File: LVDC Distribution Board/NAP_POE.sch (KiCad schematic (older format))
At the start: 0 parts

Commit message: Inputs / Outputs Reallyyyy Done
These two schematic sections are very finalized now. Time to do the power conversion section : - )
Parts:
- added J? (x2): RJ45_LED_Shielded, symbol Connector:RJ45_LED_Shielded
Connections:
- new net: J?.1, J?.1
- new net: J?.2, J?.2
- new net: J?.3, J?.3
- new net: J?.6, J?.6
- new net GND: J?.7, J?.8, J?.SH, J?.SH
- new net LP24V: J?.4, J?.5
- no-connect marks 0 -> 4
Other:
- note added: "NAP PoE"
- note added: "Should probably light the green LED on startup,\nas a debugging "she got power bys" check"
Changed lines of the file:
@@
 $Descr A4 11693 8268
 encoding utf-8
-Sheet 1 7
+Sheet 4 7
 Title ""
 Date ""
@@
 Comment4 ""
 $EndDescr
+Text Notes 8350 6960 0    197  Italic 39
+NAP PoE
+$Comp
+L Connector:RJ45_LED_Shielded J?
+U 1 1 5C650637
+P 6680 4150
+F 0 "J?" H 6680 4817 50  0000 C CNN
+F 1 "RJ45_LED_Shielded" H 6680 4726 50  0000 C CNN
+F 2 "" V 6680 4175 50  0001 C CNN
+F 3 "~" V 6680 4175 50  0001 C CNN
+	1    6680 4150
+	-1   0    0    1
+$EndComp
+$Comp
+L Connector:RJ45_LED_Shielded J?
+U 1 1 5C650693
+P 6670 2430
+F 0 "J?" H 6670 3097 50  0000 C CNN
+F 1 "RJ45_LED_Shielded" H 6670 3006 50  0000 C CNN
+F 2 "" V 6670 2455 50  0001 C CNN
+F 3 "~" V 6670 2455 50  0001 C CNN
+	1    6670 2430
+	-1   0    0    1
+$EndComp
+$Comp
+L power:GND #PWR?
+U 1 1 5C650810
+P 6890 3510
+F 0 "#PWR?" H 6890 3260 50  0001 C CNN
+F 1 "GND" H 6895 3337 50  0000 C CNN
+F 2 "" H 6890 3510 50  0001 C CNN
+F 3 "" H 6890 3510 50  0001 C CNN
+	1    6890 3510
+	1    0    0    -1
+$EndComp
+$Comp
+L power:GND #PWR?
+U 1 1 5C65082E
+P 6920 1760
+F 0 "#PWR?" H 6920 1510 50  0001 C CNN
+F 1 "GND" H 6925 1587 50  0000 C CNN
+F 2 "" H 6920 1760 50  0001 C CNN
+F 3 "" H 6920 1760 50  0001 C CNN
+	1    6920 1760
+	1    0    0    -1
+$EndComp
+Wire Wire Line
+	6890 3510 6890 3480
+Wire Wire Line
+	6890 3480 6680 3480
+Wire Wire Line
+	6680 3480 6680 3650
+Wire Wire Line
+	6920 1760 6920 1710
+Wire Wire Line
+	6920 1710 6670 1710
+Wire Wire Line
+	6670 1710 6670 1930
+NoConn ~ 6270 2830
+NoConn ~ 6270 2730
+NoConn ~ 6270 2530
+NoConn ~ 6270 2430
+Wire Wire Line
+	6270 2630 5910 2630
+Wire Wire Line
+	5910 2630 5910 4350
+Wire Wire Line
+	5910 4350 6280 4350
+Wire Wire Line
+	6270 2330 5940 2330
+Wire Wire Line
+	5940 2330 5940 4050
+Wire Wire Line
+	5940 4050 6280 4050
+Wire Wire Line
+	6270 2230 5980 2230
+Wire Wire Line
+	5980 2230 5980 3950
+Wire Wire Line
+	5980 3950 6280 3950
+Wire Wire Line
+	6270 2130 6020 2130
+Wire Wire Line
+	6020 2130 6020 3850
+Wire Wire Line
+	6020 3850 6280 3850
+Wire Wire Line
+	6280 4450 6180 4450
+Wire Wire Line
+	6180 4450 6180 4550
+Wire Wire Line
+	6180 4550 6280 4550
+Wire Wire Line
+	6180 4550 6180 4710
+Connection ~ 6180 4550
+$Comp
+L power:GND #PWR?
+U 1 1 5C65173A
+P 6180 4710
+F 0 "#PWR?" H 6180 4460 50  0001 C CNN
+F 1 "GND" H 6185 4537 50  0000 C CNN
+F 2 "" H 6180 4710 50  0001 C CNN
+F 3 "" H 6180 4710 50  0001 C CNN
+	1    6180 4710
+	1    0    0    -1
+$EndComp
+Wire Wire Line
+	6280 4150 6200 4150
+Wire Wire Line
+	6200 4150 6200 4250
+Wire Wire Line
+	6200 4250 6280 4250
+Wire Wire Line
+	6200 4150 4410 4150
+Connection ~ 6200 4150
+Text HLabel 4410 4150 0    50   Input ~ 0
+LP24V
+Text Notes 7230 2220 0    50   ~ 0
+Should probably light the green LED on startup,\nas a debugging "she got power bys" check
 $EndSCHEMATC

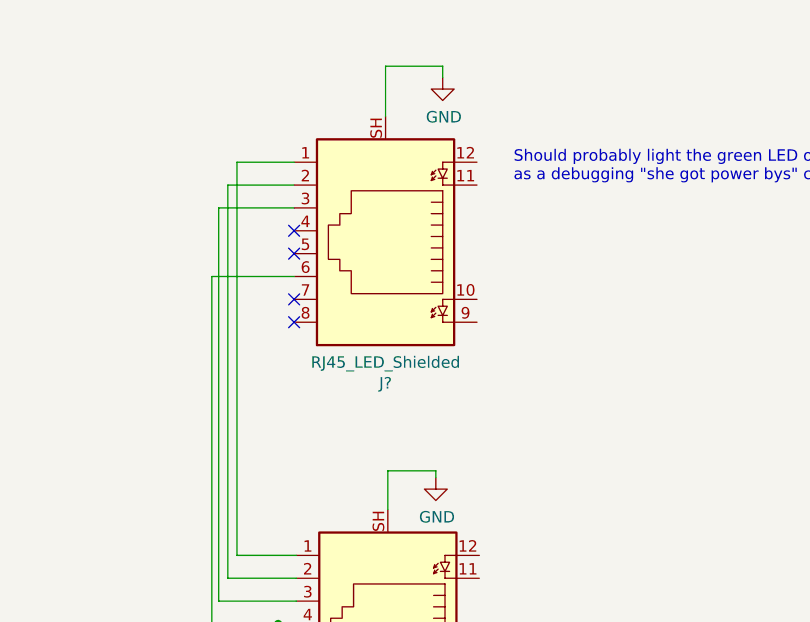
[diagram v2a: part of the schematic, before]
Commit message: SAMD21 Added
-Added VSense on rails
-Added SAMD21 and related circuits
-Mapped signals to the uC.
-Hope this is a better commit description
-Hi Frank
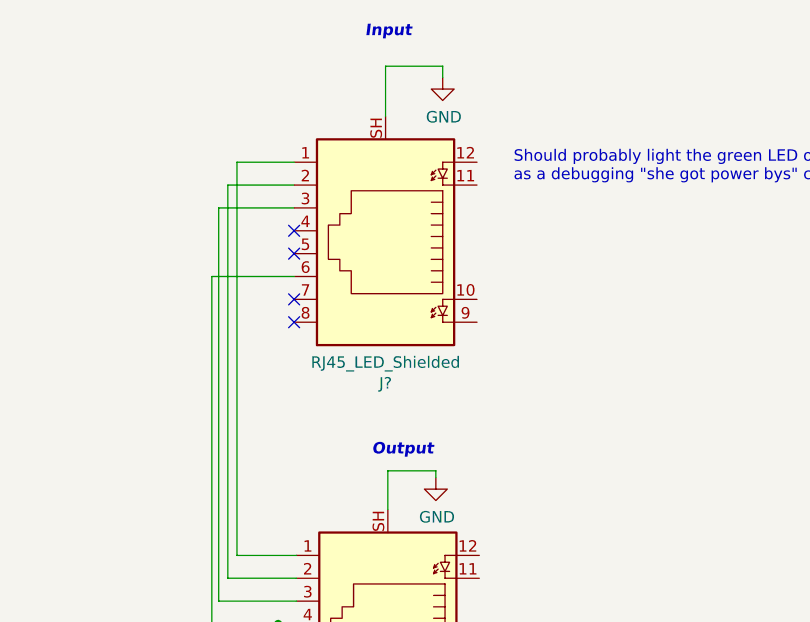
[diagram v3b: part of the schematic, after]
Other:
- note added: "Input"
- note added: "Output"
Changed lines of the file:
@@
 $EndComp
 $Comp
-L power:GND #PWR?
+L power:GND #PWR0128
 U 1 1 5C650810
 P 6890 3510
-F 0 "#PWR?" H 6890 3260 50  0001 C CNN
+F 0 "#PWR0128" H 6890 3260 50  0001 C CNN
 F 1 "GND" H 6895 3337 50  0000 C CNN
 F 2 "" H 6890 3510 50  0001 C CNN
@@
 $EndComp
 $Comp
-L power:GND #PWR?
+L power:GND #PWR0129
 U 1 1 5C65082E
 P 6920 1760
-F 0 "#PWR?" H 6920 1510 50  0001 C CNN
+F 0 "#PWR0129" H 6920 1510 50  0001 C CNN
 F 1 "GND" H 6925 1587 50  0000 C CNN
 F 2 "" H 6920 1760 50  0001 C CNN
@@
 Connection ~ 6180 4550
 $Comp
-L power:GND #PWR?
+L power:GND #PWR0130
 U 1 1 5C65173A
 P 6180 4710
-F 0 "#PWR?" H 6180 4460 50  0001 C CNN
+F 0 "#PWR0130" H 6180 4460 50  0001 C CNN
 F 1 "GND" H 6185 4537 50  0000 C CNN
 F 2 "" H 6180 4710 50  0001 C CNN
@@
 Text Notes 7230 2220 0    50   ~ 0
 Should probably light the green LED on startup,\nas a debugging "she got power bys" check
+Text Notes 6580 1590 0    50   Italic 10
+Input
+Text Notes 6610 3420 0    50   Italic 10
+Output
 $EndSCHEMATC

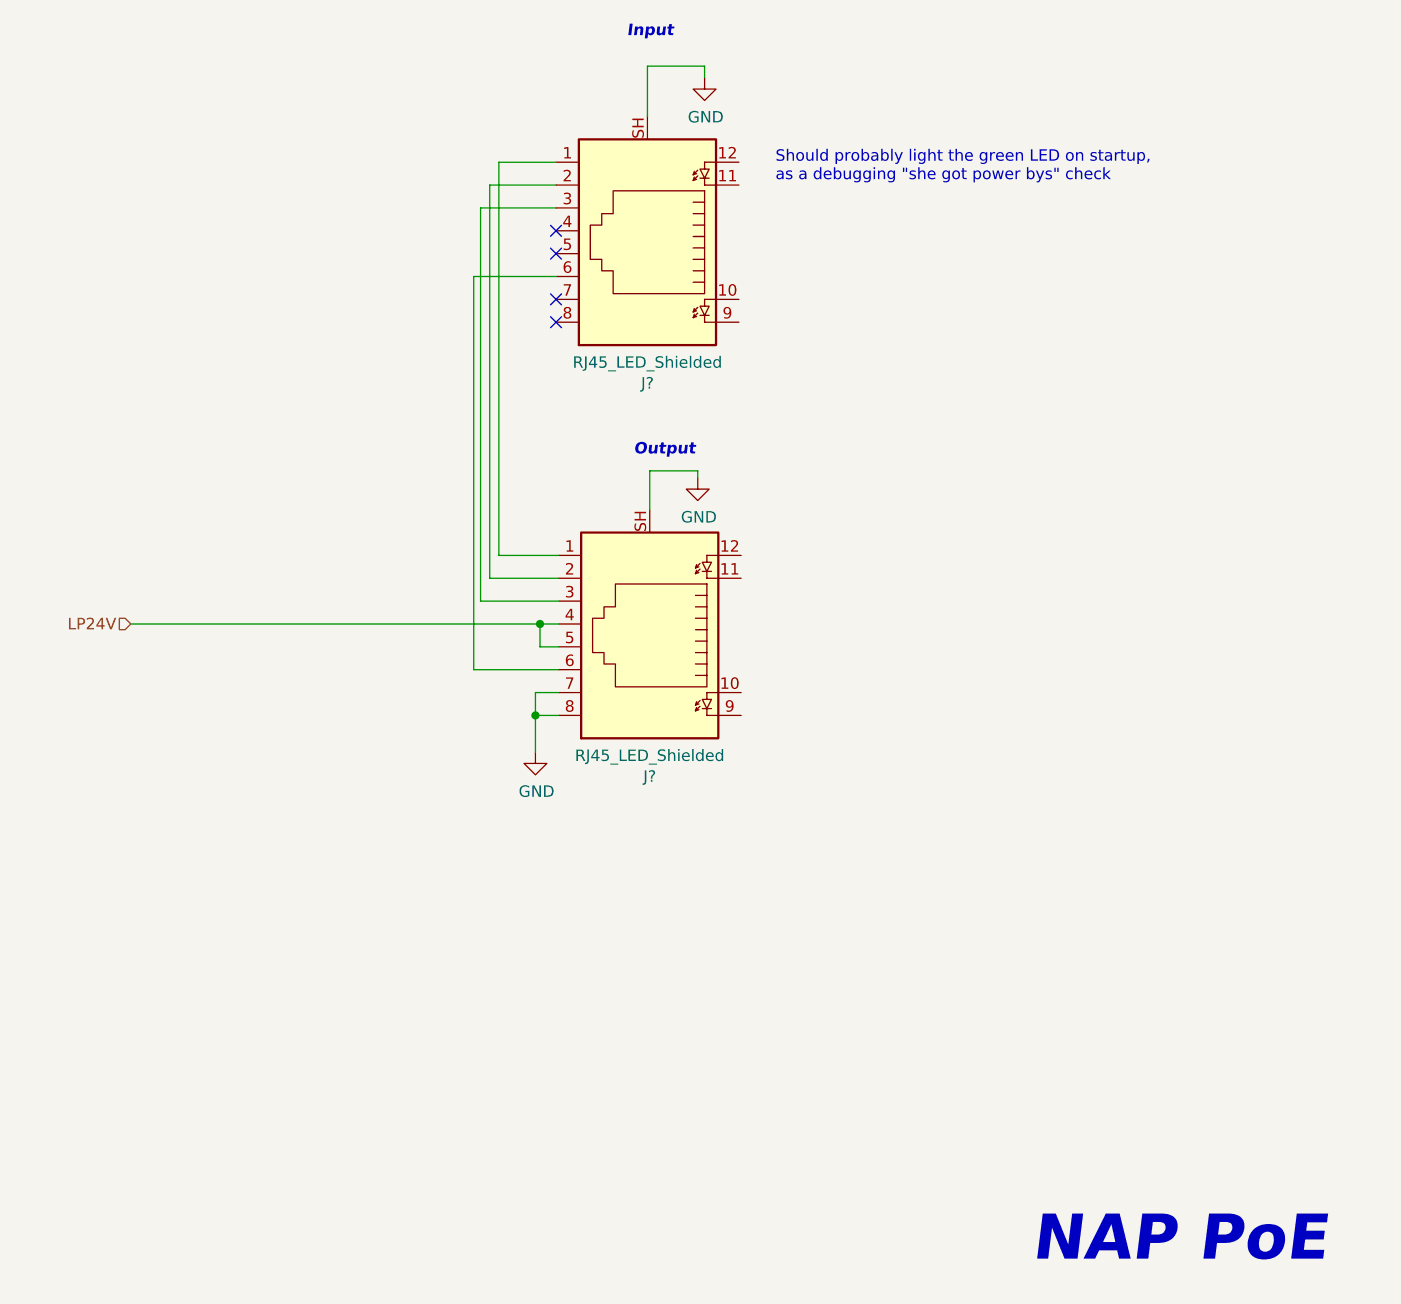
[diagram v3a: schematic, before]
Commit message: Schematic "Done"
-Added Wiznet legacy n0de schematic
-Cleaned up schematic in general
-Other than minor changes, the schematic is finalized.
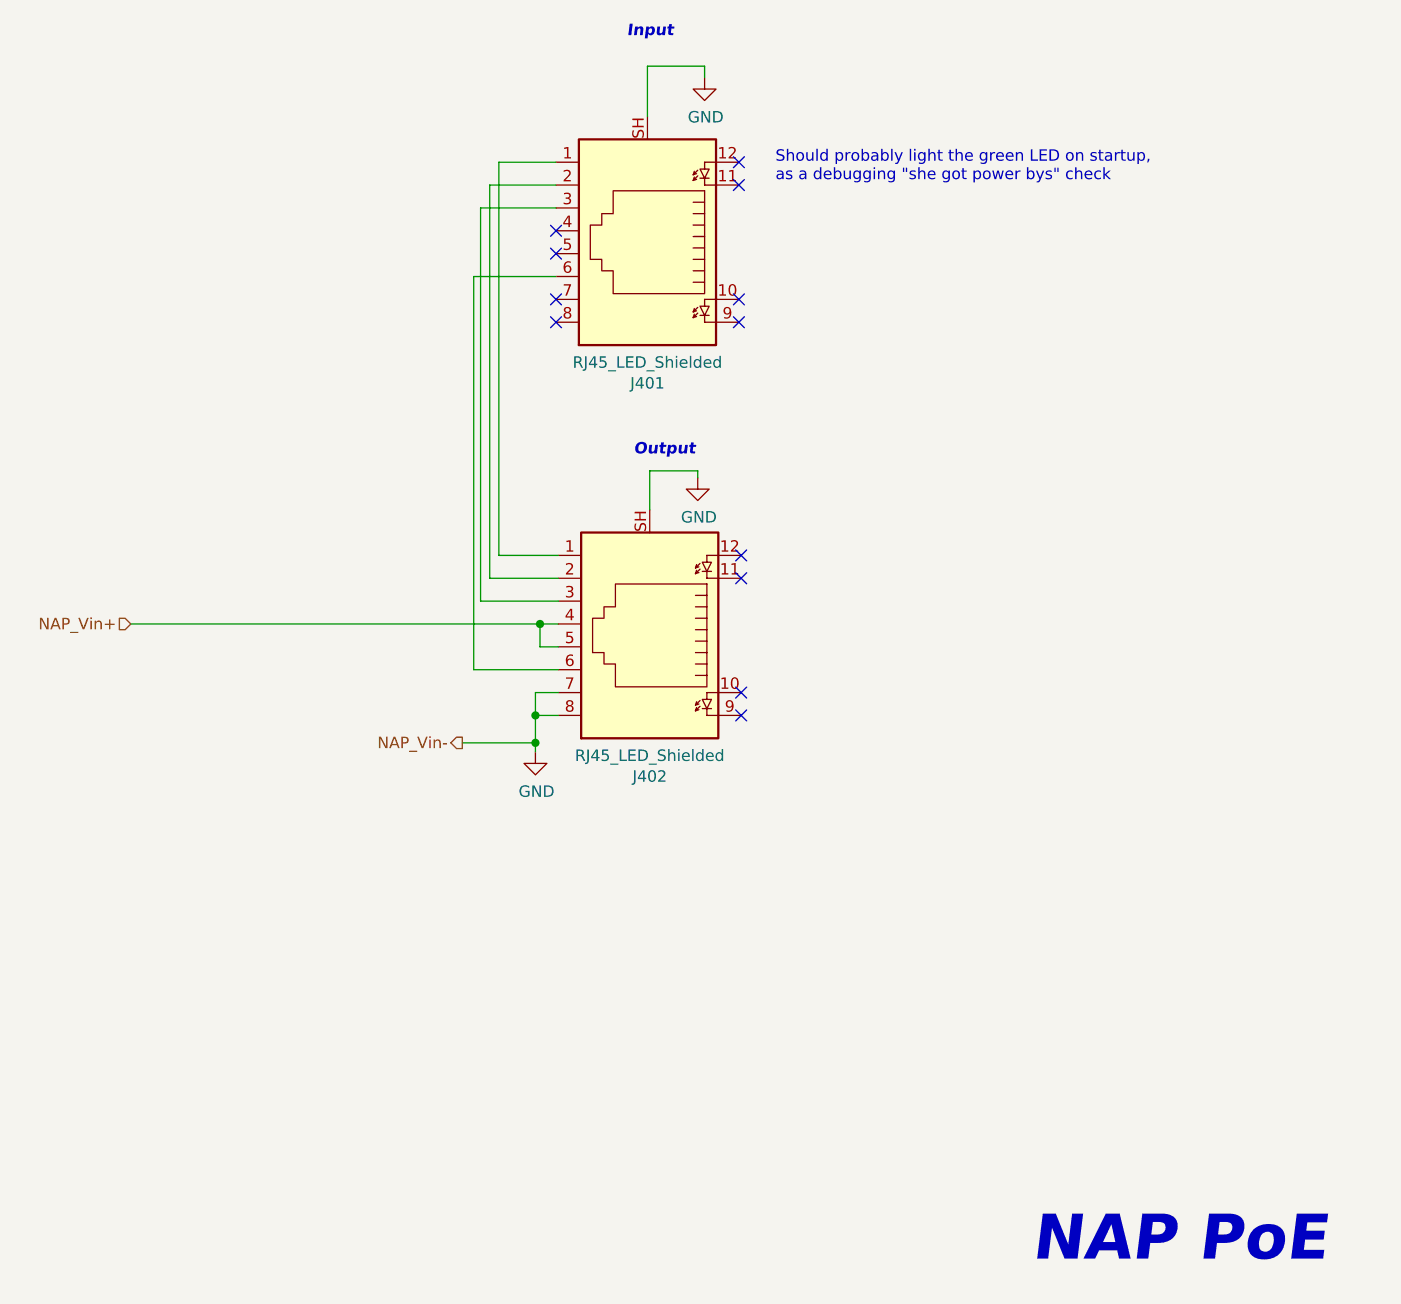
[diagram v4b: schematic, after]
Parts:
- gave numbers to parts that had none: 2
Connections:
- net LP24V renamed NAP_Vin+
- no-connect marks 4 -> 12
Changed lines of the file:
@@
 NAP PoE
 $Comp
-L Connector:RJ45_LED_Shielded J?
+L Connector:RJ45_LED_Shielded J402
 U 1 1 5C650637
 P 6680 4150
-F 0 "J?" H 6680 4817 50  0000 C CNN
+F 0 "J402" H 6680 4817 50  0000 C CNN
 F 1 "RJ45_LED_Shielded" H 6680 4726 50  0000 C CNN
 F 2 "" V 6680 4175 50  0001 C CNN
@@
 $EndComp
 $Comp
-L Connector:RJ45_LED_Shielded J?
+L Connector:RJ45_LED_Shielded J401
 U 1 1 5C650693
 P 6670 2430
-F 0 "J?" H 6670 3097 50  0000 C CNN
+F 0 "J401" H 6670 3097 50  0000 C CNN
 F 1 "RJ45_LED_Shielded" H 6670 3006 50  0000 C CNN
 F 2 "" V 6670 2455 50  0001 C CNN
@@
 	6180 4550 6280 4550
 Wire Wire Line
-	6180 4550 6180 4710
+	6180 4550 6180 4670
 Connection ~ 6180 4550
 $Comp
@@
 Connection ~ 6200 4150
 Text HLabel 4410 4150 0    50   Input ~ 0
-LP24V
+NAP_Vin+
 Text Notes 7230 2220 0    50   ~ 0
 Should probably light the green LED on startup,\nas a debugging "she got power bys" check
@@
 Text Notes 6610 3420 0    50   Italic 10
 Output
+Text HLabel 5860 4670 0    50   Output ~ 0
+NAP_Vin-
+Wire Wire Line
+	5860 4670 6180 4670
+Connection ~ 6180 4670
+Wire Wire Line
+	6180 4670 6180 4710
+NoConn ~ 7070 2130
+NoConn ~ 7070 2230
+NoConn ~ 7070 2730
+NoConn ~ 7070 2830
+NoConn ~ 7080 3850
+NoConn ~ 7080 3950
+NoConn ~ 7080 4450
+NoConn ~ 7080 4550
 $EndSCHEMATC

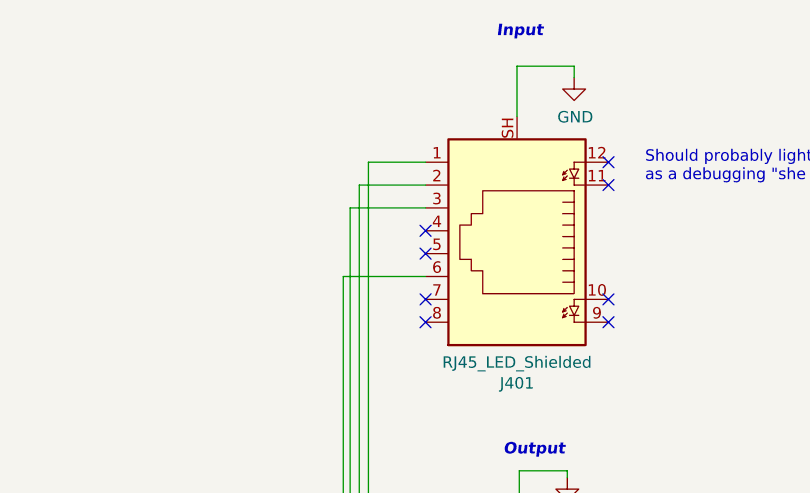
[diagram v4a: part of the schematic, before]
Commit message: Rev Protection Fix
- Added LTspice models of reverse protection.
- Fixed reverse protection circuit, verified through spice.
- Added net names to NAP PoE circuit.
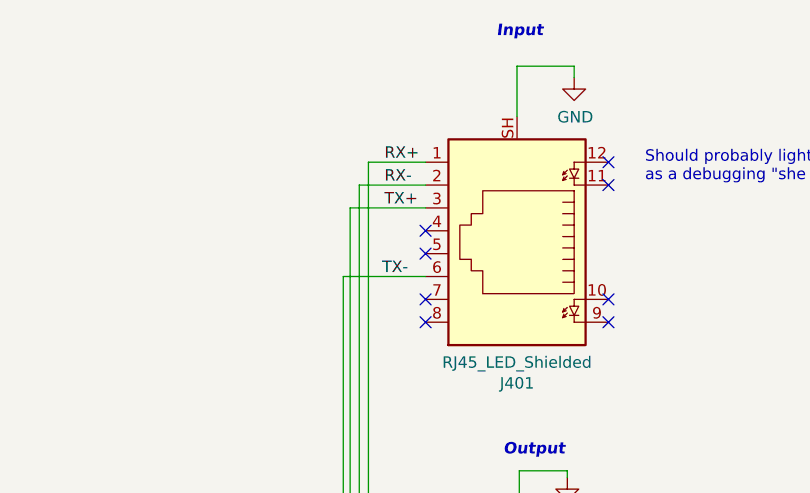
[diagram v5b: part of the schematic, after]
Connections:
- net RX+: now reaches J401.1, J402.1
- net RX-: now reaches J401.2, J402.2
- net TX+: now reaches J401.3, J402.3
- net TX-: now reaches J401.6, J402.6
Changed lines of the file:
@@
 NoConn ~ 7080 4450
 NoConn ~ 7080 4550
+Text Label 6080 2630 0    50   ~ 0
+TX-
+Text Label 6090 2330 0    50   ~ 0
+TX+
+Text Label 6090 2230 0    50   ~ 0
+RX-
+Text Label 6090 2130 0    50   ~ 0
+RX+
 $EndSCHEMATC

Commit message: Fixed library addresses and worked on LVDC layout
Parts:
- J401, J402: footprint (none) -> hyperCustom:RJ45_8P8C_90DEG_LEDs
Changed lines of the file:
@@
 F 0 "J402" H 6680 4817 50  0000 C CNN
 F 1 "RJ45_LED_Shielded" H 6680 4726 50  0000 C CNN
-F 2 "" V 6680 4175 50  0001 C CNN
+F 2 "hyperCustom:RJ45_8P8C_90DEG_LEDs" V 6680 4175 50  0001 C CNN
 F 3 "~" V 6680 4175 50  0001 C CNN
 	1    6680 4150
@@
 F 0 "J401" H 6670 3097 50  0000 C CNN
 F 1 "RJ45_LED_Shielded" H 6670 3006 50  0000 C CNN
-F 2 "" V 6670 2455 50  0001 C CNN
+F 2 "hyperCustom:RJ45_8P8C_90DEG_LEDs" V 6670 2455 50  0001 C CNN
 F 3 "~" V 6670 2455 50  0001 C CNN
 	1    6670 2430

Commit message: Annotated and references
Added annotations and references. MCU pins to be added next
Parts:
- removed J401, J402: RJ45_LED_Shielded, hyperCustom:RJ45_8P8C_90DEG_LEDs, symbol Connector:RJ45_LED_Shielded
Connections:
- no-connect marks 12 -> 0
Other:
- note removed: "Input"
- note removed: "NAP PoE"
- note removed: "Output"
- note removed: "Should probably light the green LED on startup,\nas a debugging "she got power bys" check"
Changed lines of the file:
@@
 $Descr A4 11693 8268
 encoding utf-8
-Sheet 4 8
+Sheet 4 10
 Title ""
 Date ""
@@
 Comment4 ""
 $EndDescr
-Text Notes 8350 6960 0    197  Italic 39
-NAP PoE
-$Comp
-L Connector:RJ45_LED_Shielded J402
-U 1 1 5C650637
-P 6680 4150
-F 0 "J402" H 6680 4817 50  0000 C CNN
-F 1 "RJ45_LED_Shielded" H 6680 4726 50  0000 C CNN
-F 2 "hyperCustom:RJ45_8P8C_90DEG_LEDs" V 6680 4175 50  0001 C CNN
-F 3 "~" V 6680 4175 50  0001 C CNN
-	1    6680 4150
-	-1   0    0    1
-$EndComp
-$Comp
-L Connector:RJ45_LED_Shielded J401
-U 1 1 5C650693
-P 6670 2430
-F 0 "J401" H 6670 3097 50  0000 C CNN
-F 1 "RJ45_LED_Shielded" H 6670 3006 50  0000 C CNN
-F 2 "hyperCustom:RJ45_8P8C_90DEG_LEDs" V 6670 2455 50  0001 C CNN
-F 3 "~" V 6670 2455 50  0001 C CNN
-	1    6670 2430
-	-1   0    0    1
-$EndComp
-$Comp
-L power:GND #PWR0128
-U 1 1 5C650810
-P 6890 3510
-F 0 "#PWR0128" H 6890 3260 50  0001 C CNN
-F 1 "GND" H 6895 3337 50  0000 C CNN
-F 2 "" H 6890 3510 50  0001 C CNN
-F 3 "" H 6890 3510 50  0001 C CNN
-	1    6890 3510
-	1    0    0    -1
-$EndComp
-$Comp
-L power:GND #PWR0129
-U 1 1 5C65082E
-P 6920 1760
-F 0 "#PWR0129" H 6920 1510 50  0001 C CNN
-F 1 "GND" H 6925 1587 50  0000 C CNN
-F 2 "" H 6920 1760 50  0001 C CNN
-F 3 "" H 6920 1760 50  0001 C CNN
-	1    6920 1760
-	1    0    0    -1
-$EndComp
-Wire Wire Line
-	6890 3510 6890 3480
-Wire Wire Line
-	6890 3480 6680 3480
-Wire Wire Line
-	6680 3480 6680 3650
-Wire Wire Line
-	6920 1760 6920 1710
-Wire Wire Line
-	6920 1710 6670 1710
-Wire Wire Line
-	6670 1710 6670 1930
-NoConn ~ 6270 2830
-NoConn ~ 6270 2730
-NoConn ~ 6270 2530
-NoConn ~ 6270 2430
-Wire Wire Line
-	6270 2630 5910 2630
-Wire Wire Line
-	5910 2630 5910 4350
-Wire Wire Line
-	5910 4350 6280 4350
-Wire Wire Line
-	6270 2330 5940 2330
-Wire Wire Line
-	5940 2330 5940 4050
-Wire Wire Line
-	5940 4050 6280 4050
-Wire Wire Line
-	6270 2230 5980 2230
-Wire Wire Line
-	5980 2230 5980 3950
-Wire Wire Line
-	5980 3950 6280 3950
-Wire Wire Line
-	6270 2130 6020 2130
-Wire Wire Line
-	6020 2130 6020 3850
-Wire Wire Line
-	6020 3850 6280 3850
-Wire Wire Line
-	6280 4450 6180 4450
-Wire Wire Line
-	6180 4450 6180 4550
-Wire Wire Line
-	6180 4550 6280 4550
-Wire Wire Line
-	6180 4550 6180 4670
-Connection ~ 6180 4550
-$Comp
-L power:GND #PWR0130
-U 1 1 5C65173A
-P 6180 4710
-F 0 "#PWR0130" H 6180 4460 50  0001 C CNN
-F 1 "GND" H 6185 4537 50  0000 C CNN
-F 2 "" H 6180 4710 50  0001 C CNN
-F 3 "" H 6180 4710 50  0001 C CNN
-	1    6180 4710
-	1    0    0    -1
-$EndComp
-Wire Wire Line
-	6280 4150 6200 4150
-Wire Wire Line
-	6200 4150 6200 4250
-Wire Wire Line
-	6200 4250 6280 4250
-Wire Wire Line
-	6200 4150 4410 4150
-Connection ~ 6200 4150
-Text HLabel 4410 4150 0    50   Input ~ 0
-NAP_Vin+
-Text Notes 7230 2220 0    50   ~ 0
-Should probably light the green LED on startup,\nas a debugging "she got power bys" check
-Text Notes 6580 1590 0    50   Italic 10
-Input
-Text Notes 6610 3420 0    50   Italic 10
-Output
-Text HLabel 5860 4670 0    50   Output ~ 0
-NAP_Vin-
-Wire Wire Line
-	5860 4670 6180 4670
-Connection ~ 6180 4670
-Wire Wire Line
-	6180 4670 6180 4710
-NoConn ~ 7070 2130
-NoConn ~ 7070 2230
-NoConn ~ 7070 2730
-NoConn ~ 7070 2830
-NoConn ~ 7080 3850
-NoConn ~ 7080 3950
-NoConn ~ 7080 4450
-NoConn ~ 7080 4550
-Text Label 6080 2630 0    50   ~ 0
-TX-
-Text Label 6090 2330 0    50   ~ 0
-TX+
-Text Label 6090 2230 0    50   ~ 0
-RX-
-Text Label 6090 2130 0    50   ~ 0
-RX+
 $EndSCHEMATC
